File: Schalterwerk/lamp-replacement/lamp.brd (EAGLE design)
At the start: 51 x 35 mm, 7 parts

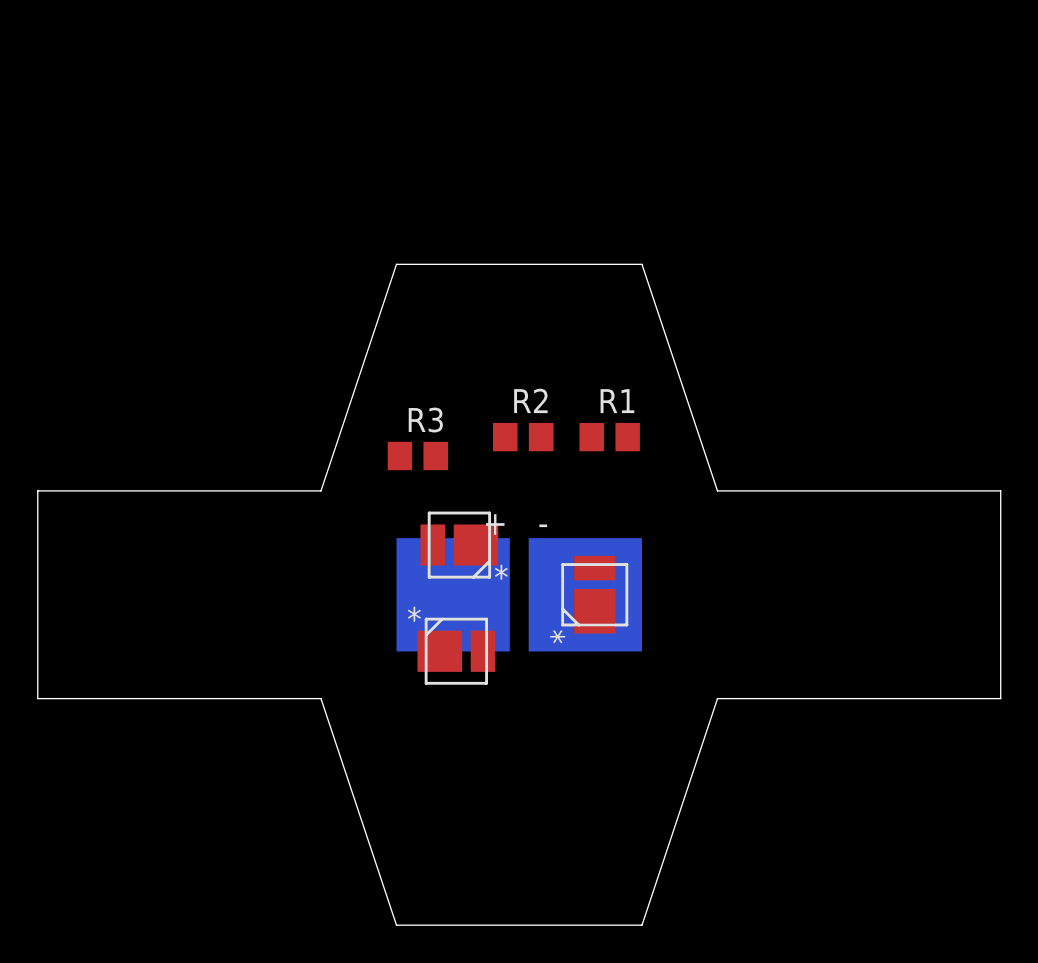
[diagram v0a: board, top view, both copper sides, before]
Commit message: Finishes layout of the lamp circuit.
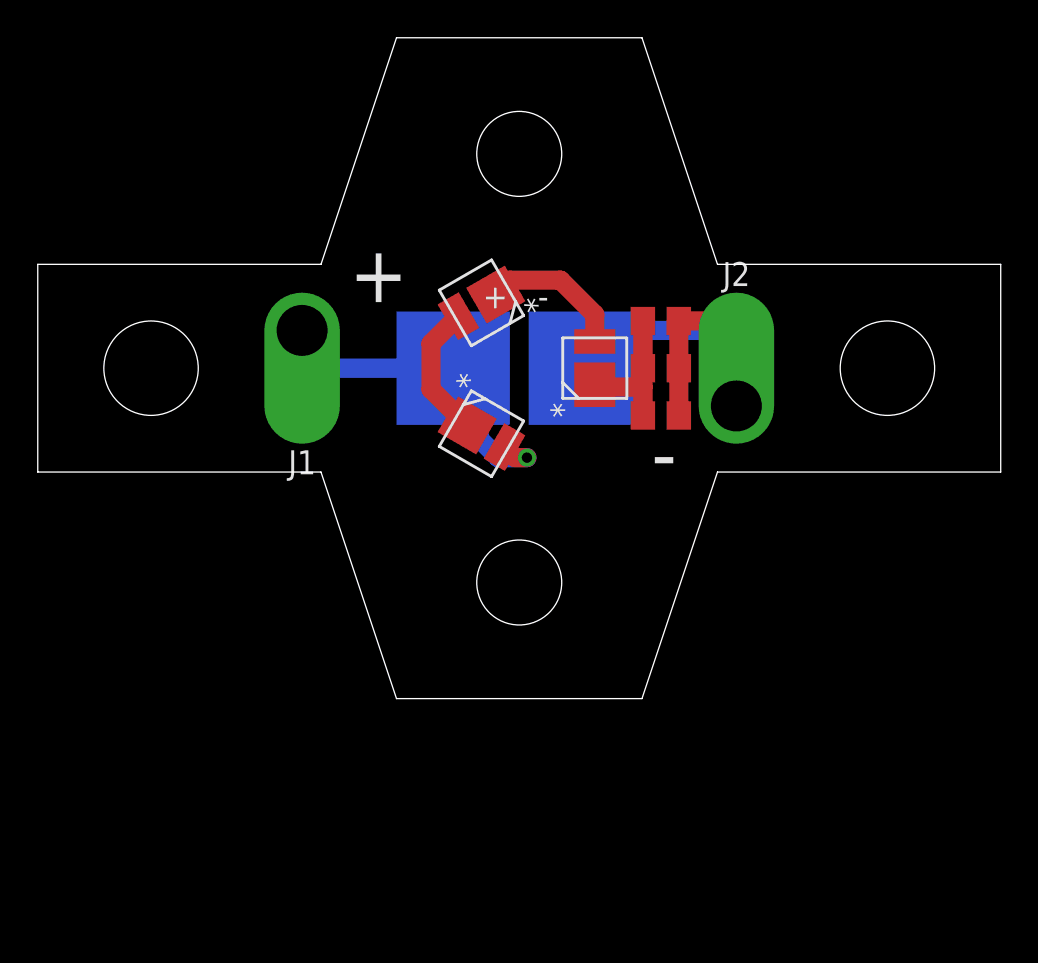
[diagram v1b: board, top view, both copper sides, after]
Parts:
- added J1, J2: (no value), eagleparts:LARGE-SOLDERPAD
- moved R3 14.7 mm to (33.0, 20.0), turned to 180 degrees
- moved LED2 12.9 mm to (23.5, 21.0), turned to 210 degrees
- moved LED3 12.0 mm to (29.5, 17.5)
- moved U$1 12.0 mm to (25.5, 17.5)
- moved LED1 11.6 mm to (23.5, 14.0), turned to 330 degrees
- moved R2 7.38 mm to (33.0, 15.0), turned to 180 degrees
- moved R1 4.55 mm to (33.0, 17.5), turned to 180 degrees
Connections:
- removed net N$3: LED1.2, U$1.+
- removed net N$5: R1.1, R2.1, R3.1, U$1.-
- new net +12V: J1.P$1, LED1.2, U$1.+
- new net GND: J2.P$1, R1.1, R2.1, R3.1, U$1.-
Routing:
- net GND: track 0.00 -> 28.7 mm
- net +12V: track 0.00 -> 18.7 mm, vias 0 -> 1
- net N$2: track 0.00 -> 7.74 mm
- net N$4: track 0.00 -> 7.71 mm
- net N$1: track 0.00 -> 7.18 mm
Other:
- board text added: "+"
- board text added: "-"

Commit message: adds supports for vertical pipe.
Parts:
- added R4, R5: (no value), rcl:R0805
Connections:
- net GND: now also R4.1, R5.1
- net N$4: now also R4.2, R5.2
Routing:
- net GND: track 28.7 -> 33.7 mm
- net N$4: track 7.71 -> 12.7 mm
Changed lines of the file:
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@@
 <hole x="25.5" y="28.85" drill="4.5"/>
 <hole x="25.5" y="6.15" drill="4.5"/>
-<text x="16.5" y="21" size="3" layer="25" font="vector">+</text>
-<text x="32.5" y="11.5" size="3" layer="25" font="vector">-</text>
+<text x="9" y="20" size="3" layer="25" font="vector">+</text>
+<text x="39.5" y="13" size="3" layer="25" font="vector">-</text>
 </plain>
 <attributes>
@@
 </class>
 </classes>
-<designrules name="default">
+<designrules name="SeeedStudio_2layer_DRU_no_angle_20140221">
 <description language="de">&lt;b&gt;EAGLE Design Rules&lt;/b&gt;
 &lt;p&gt;
@@
 necessary adjustments and save your customized
 design rules under a new name.</description>
+<description language="zh">&lt;b&gt;Seeed Studio EAGLE Design Rules&lt;/b&gt;
+</description>
 <param name="layerSetup" value="(1*16)"/>
-<param name="mtCopper" value="0.035mm 0.035mm 0.035mm 0.035mm 0.035mm 0.035mm 0.035mm 0.035mm 0.035mm 0.035mm 0.035mm 0.035mm 0.035mm 0.035mm 0.035mm 0.035mm"/>
-<param name="mtIsolate" value="1.5mm 0.15mm 0.2mm 0.15mm 0.2mm 0.15mm 0.2mm 0.15mm 0.2mm 0.15mm 0.2mm 0.15mm 0.2mm 0.15mm 0.2mm"/>
+<param name="mtCopper" value="0.035mm 0.0175mm 0.035mm 0.035mm 0.035mm 0.035mm 0.035mm 0.035mm 0.035mm 0.035mm 0.035mm 0.035mm 0.035mm 0.035mm 0.0175mm 0.035mm"/>
+<param name="mtIsolate" value="1.5mm 1.1mm 0.2mm 0.15mm 0.2mm 0.15mm 0.2mm 0.15mm 0.2mm 0.15mm 0.2mm 0.15mm 0.2mm 0.15mm 0.2mm"/>
 <param name="mdWireWire" value="6mil"/>
 <param name="mdWirePad" value="6mil"/>
@@
 <param name="mdPadVia" value="6mil"/>
 <param name="mdViaVia" value="6mil"/>
-<param name="mdSmdPad" value="6mil"/>
-<param name="mdSmdVia" value="6mil"/>
-<param name="mdSmdSmd" value="6mil"/>
-<param name="mdViaViaSameLayer" value="6mil"/>
+<param name="mdSmdPad" value="0mil"/>
+<param name="mdSmdVia" value="0mil"/>
+<param name="mdSmdSmd" value="0mil"/>
+<param name="mdViaViaSameLayer" value="8mil"/>
 <param name="mnLayersViaInSmd" value="2"/>
-<param name="mdCopperDimension" value="40mil"/>
-<param name="mdDrill" value="6mil"/>
+<param name="mdCopperDimension" value="10mil"/>
+<param name="mdDrill" value="10mil"/>
 <param name="mdSmdStop" value="0mil"/>
 <param name="msWidth" value="6mil"/>
-<param name="msDrill" value="0.35mm"/>
-<param name="msMicroVia" value="9.99mm"/>
+<param name="msDrill" value="12mil"/>
+<param name="msMicroVia" value="12mil"/>
 <param name="msBlindViaRatio" value="0.5"/>
 <param name="rvPadTop" value="0.25"/>
@@
 <param name="rlMinPadBottom" value="10mil"/>
 <param name="rlMaxPadBottom" value="20mil"/>
-<param name="rlMinViaOuter" value="8mil"/>
+<param name="rlMinViaOuter" value="6mil"/>
 <param name="rlMaxViaOuter" value="20mil"/>
-<param name="rlMinViaInner" value="8mil"/>
+<param name="rlMinViaInner" value="6mil"/>
 <param name="rlMaxViaInner" value="20mil"/>
 <param name="rlMinMicroViaOuter" value="4mil"/>
@@
 <param name="psTop" value="-1"/>
 <param name="psBottom" value="-1"/>
-<param name="psFirst" value="-1"/>
+<param name="psFirst" value="0"/>
 <param name="psElongationLong" value="100"/>
 <param name="psElongationOffset" value="100"/>
 <param name="mvStopFrame" value="1"/>
 <param name="mvCreamFrame" value="0"/>
-<param name="mlMinStopFrame" value="4mil"/>
-<param name="mlMaxStopFrame" value="4mil"/>
+<param name="mlMinStopFrame" value="2mil"/>
+<param name="mlMaxStopFrame" value="2mil"/>
 <param name="mlMinCreamFrame" value="0mil"/>
 <param name="mlMaxCreamFrame" value="0mil"/>
-<param name="mlViaStopLimit" value="0mil"/>
+<param name="mlViaStopLimit" value="100mil"/>
 <param name="srRoundness" value="0"/>
 <param name="srMinRoundness" value="0mil"/>
@@
 <param name="checkAngle" value="0"/>
 <param name="checkFont" value="1"/>
-<param name="checkRestrict" value="1"/>
+<param name="checkRestrict" value="0"/>
 <param name="checkStop" value="0"/>
 <param name="checkValues" value="0"/>
@@
 <element name="U$1" library="eagleparts" package="LED-BOARD-IN" value="LED-BOARD-IN" x="25.5" y="17.5" smashed="yes" rot="MR180"/>
 <element name="J1" library="eagleparts" package="LARGE-SOLDERPAD" value="" x="14" y="19.5" smashed="yes" rot="R180">
-<attribute name="NAME" x="14" y="13.15" size="1.27" layer="21" rot="R180" align="bottom-center"/>
 <attribute name="VALUE" x="14" y="22.04" size="1.27" layer="27" rot="R180" align="top-center"/>
 </element>
 <element name="J2" library="eagleparts" package="LARGE-SOLDERPAD" value="" x="37" y="15.5" smashed="yes">
-<attribute name="NAME" x="37" y="21.85" size="1.27" layer="21" align="bottom-center"/>
 <attribute name="VALUE" x="37" y="12.96" size="1.27" layer="27" align="top-center"/>
+</element>
+<element name="R4" library="rcl" library_urn="urn:adsk.eagle:library:334" package="R0805" package3d_urn="urn:adsk.eagle:package:23553/2" value="" x="33" y="22.5" smashed="yes" rot="R180">
+<attribute name="POPULARITY" value="86" x="33" y="22.5" size="3" layer="27" font="vector" rot="R180" display="off"/>
+<attribute name="SPICEPREFIX" value="R" x="33" y="22.5" size="3" layer="27" font="vector" rot="R180" display="off"/>
+<attribute name="VALUE" x="33.635" y="25.04" size="1.27" layer="27" rot="R180"/>
+</element>
+<element name="R5" library="rcl" library_urn="urn:adsk.eagle:library:334" package="R0805" package3d_urn="urn:adsk.eagle:package:23553/2" value="" x="33" y="12.5" smashed="yes" rot="R180">
+<attribute name="POPULARITY" value="86" x="33" y="12.5" size="3" layer="27" font="vector" rot="R180" display="off"/>
+<attribute name="SPICEPREFIX" value="R" x="33" y="12.5" size="3" layer="27" font="vector" rot="R180" display="off"/>
+<attribute name="VALUE" x="33.635" y="15.04" size="1.27" layer="27" rot="R180"/>
 </element>
 </elements>
@@
 <contactref element="LED2" pad="1"/>
 <contactref element="LED3" pad="2"/>
-<wire x1="24.258896875" y1="21.39815" x2="25.020746875" y2="22.16" width="1.016" layer="1"/>
+<wire x1="24.258896875" y1="21.39815" x2="24.639746875" y2="21.779" width="1.016" layer="1"/>
 <wire x1="29.5" y1="20.346" x2="29.5" y2="18.9097" width="1.016" layer="1"/>
-<wire x1="25.020746875" y1="22.16" x2="27.686" y2="22.16" width="1.016" layer="1"/>
-<wire x1="27.686" y1="22.16" x2="29.5" y2="20.346" width="1.016" layer="1"/>
+<wire x1="24.639746875" y1="21.779" x2="28.067" y2="21.779" width="1.016" layer="1"/>
+<wire x1="28.067" y1="21.779" x2="29.5" y2="20.346" width="1.016" layer="1"/>
 </signal>
 <signal name="N$4">
@@
 <wire x1="29.5" y1="16.6237" x2="29.6237" y2="16.5" width="1.016" layer="1"/>
 <wire x1="29.6237" y1="16.5" x2="32.05" y2="16.5" width="1.016" layer="1"/>
+<contactref element="R4" pad="2"/>
+<contactref element="R5" pad="2"/>
+<wire x1="32.05" y1="22.5" x2="32.05" y2="20" width="1.016" layer="1"/>
+<wire x1="32.05" y1="12.5" x2="32.05" y2="15" width="1.016" layer="1"/>
 </signal>
 <signal name="GND">
@@
 <wire x1="31" y1="19.5" x2="37" y2="19.5" width="1.016" layer="16"/>
 <wire x1="37" y1="19.5" x2="37" y2="15.5" width="1.016" layer="16"/>
+<contactref element="R4" pad="1"/>
+<contactref element="R5" pad="1"/>
+<wire x1="33.95" y1="22.5" x2="33.95" y2="20" width="1.016" layer="1"/>
+<wire x1="33.95" y1="12.5" x2="33.95" y2="15" width="1.016" layer="1"/>
 </signal>
 <signal name="+12V">
@@
 <wire x1="14" y1="17.5" x2="14" y2="19.5" width="1.016" layer="16"/>
 </signal>
+<signal name="N$3">
+<via x="30" y="24" extent="1-16" drill="0.9"/>
+</signal>
+<signal name="N$5">
+<via x="25.5" y="25.5" extent="1-16" drill="0.9"/>
+</signal>
+<signal name="N$6">
+<via x="21" y="24" extent="1-16" drill="0.9"/>
+</signal>
+<signal name="N$7">
+<via x="21" y="11" extent="1-16" drill="0.9"/>
+</signal>
+<signal name="N$8">
+<via x="30" y="11" extent="1-16" drill="0.9"/>
+</signal>
+<signal name="N$9">
+<via x="25.5" y="9.5" extent="1-16" drill="0.9"/>
+</signal>
 </signals>
